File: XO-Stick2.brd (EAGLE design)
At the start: 74.9 x 53.3 mm, 31 parts, among them J1 POWER, J2 85MOTR, J3 85MOTL, J4 REF, J5 SCL, J6 SDA, J7 AVCC (N/C), J8 AGND (N/C), J9 EXT VCC, SW1 USER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

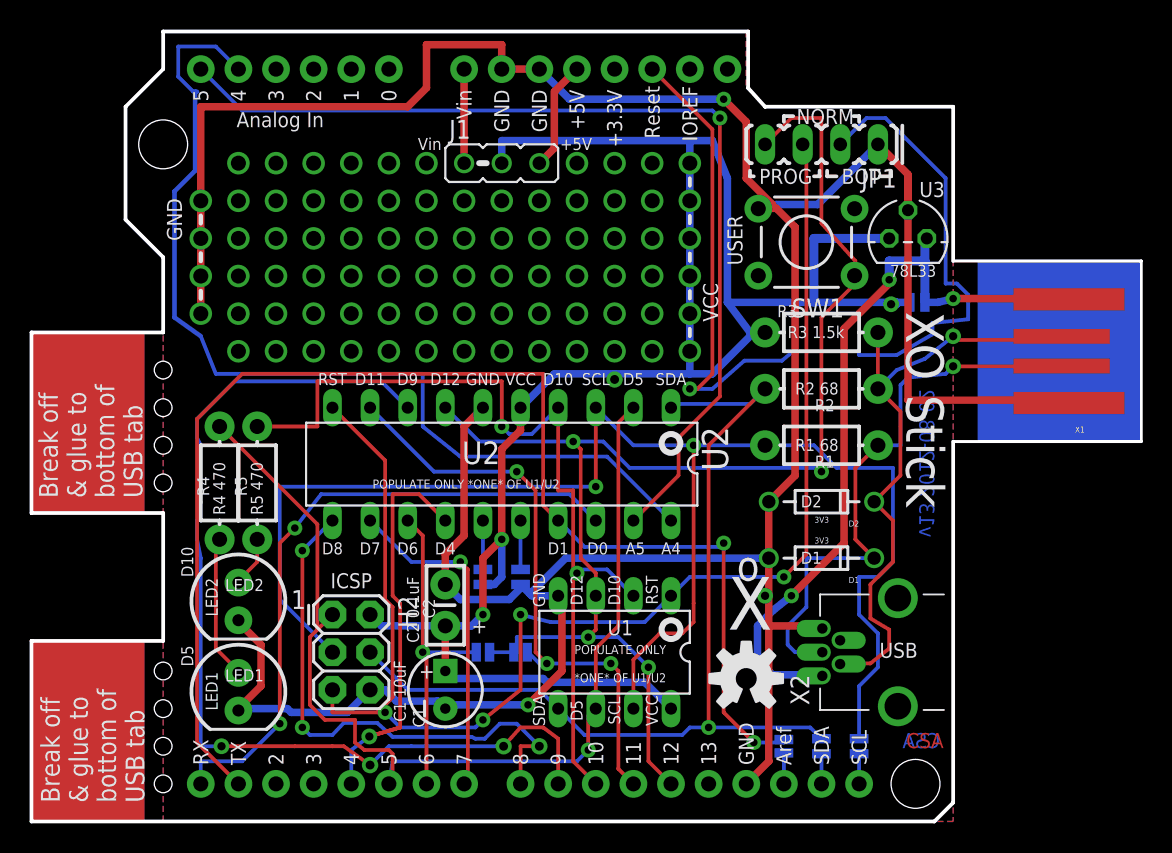
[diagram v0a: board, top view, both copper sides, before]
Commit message: XO Stick v14: move USB to PB3/4 (Louis Beaudoin suggestion).
This allows more straightforward use of the XO Stick as a programmer,
and of the XO Stick's I2C bus.

It complicates use of the '85 to drive the XOrduino bot, but that's probably
a reasonable sacrifice.
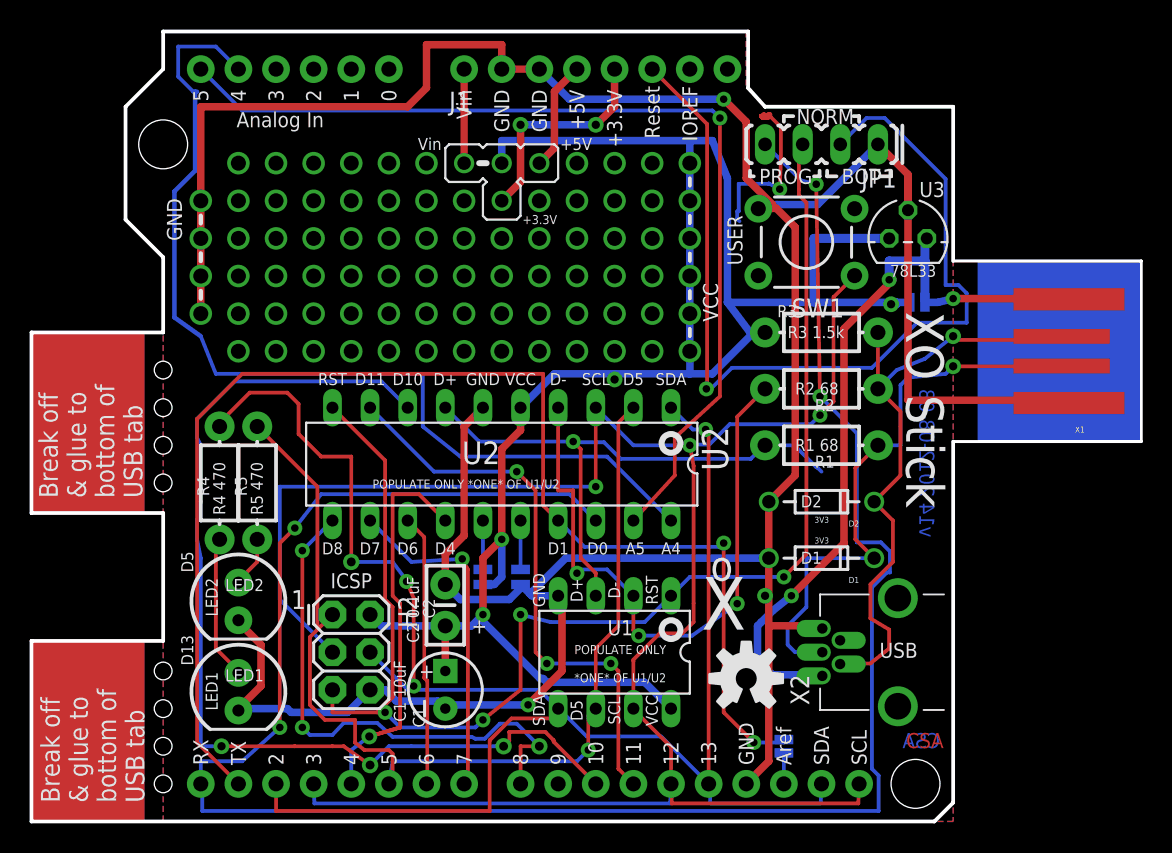
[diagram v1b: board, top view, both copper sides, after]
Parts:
- removed J2: 85MOTR, xorduino:SJ-2S-NO
- removed J3: 85MOTL, xorduino:SJ-2S-NO
- removed J5: SCL, xorduino:SJ-2S-BOT-TRACE-NOCONFLICT-PAD
- removed J6: SDA, xorduino:SJ-2S-BOT-TRACE-NOCONFLICT-PAD
- J1: device xorduino:JP3-TRACE-NOCONFLICT -> xorduino:JP4-TRACE-NOCONFLICT
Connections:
- removed net D_M: H2.4, J6.2, R2.P$2, U1.5, U2.1
- removed net D_P: H2.3, J5.2, R1.P$2, U1.7, U2.3
- removed net SCL: H1.SCL, J5.1
- removed net SDA: H1.SDA, J6.1
- new net ARD_3.3V: H1.3.3V, J1.N/O2
- new net PB0: H1.D13, H1.D2, H1.SDA, H2.4, R4.P$2, U1.5, U2.1
- new net PB2: H1.D12, H1.D3, H1.SCL, H2.3, SW1.1, U1.7, U2.3
- net ARD_5V: now also J1.N/O1; no longer J1.N/O
- net PA2: now also JP1.4
- net PA5: no longer J2.1
- net PB1: now also R5.P$2; no longer R4.P$2
- net PB3: now also R2.P$2; no longer H1.D10, R5.P$2
- net PB4: now also R1.P$2; no longer H1.D12, J2.2, J3.1, JP1.4, SW1.1
- net PB5: now also H1.D10; no longer H1.D9
- net PB6: no longer J3.2
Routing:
- net PB2: track 0.00 -> 135.2 mm, vias 0 -> 3
- net PB0: track 0.00 -> 122.6 mm, vias 0 -> 4
- net D_P: track 102.5 -> 0.00 mm, vias 2 -> 0
- net PA2: track 43.7 -> 141.9 mm, vias 2 -> 4
- net D_M: track 64.6 -> 0.00 mm, vias 1 -> 0
- net PB4: track 92.5 -> 39.0 mm, vias 4 -> 1
- net XYZ: track 0.00 -> 48.9 mm, vias 0 -> 1
- net PB3: track 59.3 -> 42.6 mm, vias 2 -> 3
- net ARD_3.3V: track 0.00 -> 15.0 mm, vias 0 -> 2
- net PA5: track 21.9 -> 18.3 mm, vias 1 -> 0
- net ARD_RST: track 65.5 -> 62.9 mm
- net SDA: track 2.03 -> 0.00 mm
- net SCL: track 2.03 -> 0.00 mm
- net PB6: track 40.2 -> 38.6 mm
- net PB1: track 72.6 -> 71.5 mm
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- added copper zone on layer 1, net GND
- added copper zone on layer 15, net GND
- removed copper zone on layer 1, net VCC
- removed copper zone on layer 15, net VCC
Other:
- board text added: "+3.3V"
- board text added: "D+"
- board text added: "D-"
- board text added: "D13"
- board text added: "v14 2012-08-08"
- board text removed: "D12"
- board text removed: "D9"
- board text removed: "L"
- board text removed: "PB4->MOTORS"
- board text removed: "R"
- board text removed: "SCL/"
- board text removed: "SDA/"
- board text removed: "v13 2012-08-02"
